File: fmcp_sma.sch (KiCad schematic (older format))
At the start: 52 parts, among them J101 Conn_Coaxial, J102 Conn_Coaxial, J103 Conn_Coaxial, J104 Conn_Coaxial, J105 Conn_Coaxial, J106 Conn_Coaxial, J201 FMCP_VITA57.4, U201 AT24C512C

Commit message: adding smas
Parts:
- removed J101, J102, J103, J104, J105, J106: Conn_Coaxial, Connector_Coaxial:MMCX_Molex_73415-0961_Horizontal_1.6mm-PCB, symbol Connector:Conn_Coaxial
- added C? (x4): 0.1uF, Capacitor_SMD:C_0201_0603Metric, symbol Device:C
- added J? (x14): Conn_Coaxial, Connector_Coaxial:MMCX_Molex_73415-0961_Horizontal_1.6mm-PCB, symbol Connector:Conn_Coaxial
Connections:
- net DPCLK_M2C_N0: now also J?.1 (In)
- net DPCLK_M2C_P0: now also J?.1 (In)
- net DP_C2M_N0: now also J?.1 (In)
- net DP_C2M_P0: now also J?.1 (In)
- net DP_M2C_N0: now also C?.2, J?.1 (In); no longer J201.C7 (DP0_M2C_N)
- net DP_M2C_P0: now also C?.2, J?.1 (In); no longer J201.C6 (DP0_M2C_P)
- net GND: now also J?.2 (Ext), J?.2 (Ext), J?.2 (Ext), J?.2 (Ext), J?.2 (Ext), J?.2 (Ext), J?.2 (Ext), J?.2 (Ext), J?.2 (Ext), J?.2 (Ext), J?.2 (Ext), J?.2 (Ext), J?.2 (Ext), J?.2 (Ext)
- net LA01_N: now also J?.1 (In)
- net LA01_P: now also J?.1 (In)
- net LA03_N: now reaches J201.G10 (LA03_N)
- net LA03_N: now also J?.1 (In)
- net LA00_P: now reaches J201.G6 (LA00_P_CC)
- net LA00_P: now also C102.2
- net LA00_N: now reaches J201.G7 (LA00_N_CC)
- net LA00_N: now also C101.2
- net LA03_P: now reaches J201.G9 (LA03_P)
- net LA03_P: now also J?.1 (In)
- net LA02_P: now reaches J201.H7 (LA02_P)
- net LA02_P: now also C?.2
- net LA02_N: now reaches J201.H8 (LA02_N)
- net LA02_N: now also C?.2
- net FPGA_CLK_C2M_C_N renamed LA00_C_N
- net LA00_C_N: now also J?.1 (In)
- net FPGA_CLK_C2M_C_P renamed LA00_C_P
- net LA00_C_P: now also J?.1 (In)
- new net: C?.1, J201.C6 (DP0_M2C_P)
- new net: C?.1, J201.C7 (DP0_M2C_N)
- new net LA02_C_N: C?.1, J?.1 (In)
- new net LA02_C_P: C?.1, J?.1 (In)
- no-connect marks 186 -> 282
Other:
- moved on the sheet: C101, C102, J201B, J201D, J201E, J201F

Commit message: added pdf
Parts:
- removed C202, C204, C207, C209: 10uF, Capacitor_SMD:C_0805_2012Metric, symbol Device:C
- removed C203, C205, C206, C208: 22uF, Capacitor_SMD:C_1210_3225Metric, symbol Device:C
- removed C210, C211, C212: C, Capacitor_SMD:C_0402_1005Metric, symbol Device:C
- removed R204, R207, R210: 0.1, Resistor_SMD:R_1210_3225Metric, symbol Device:R
- removed R205, R206, R208, R209, R211, R212: 10, Resistor_SMD:R_0402_1005Metric, symbol Device:R
- removed TP103, TP104: TestPoint, TestPoint:TestPoint_Loop_D2.50mm_Drill1.0mm, symbol Connector:TestPoint
- removed TP201, TP202, TP203: TestPoint_Probe, TestPoint:TestPoint_Pad_D1.0mm, symbol Connector:TestPoint_Probe
- removed U201: AT24C512C, Package_DFN_QFN:DFN-8-1EP_3x2mm_P0.5mm_EP1.3x1.5mm, symbol Memory_EEPROM:AT24CS64-MAHM
- added U101: M24C02-FDW, Package_SO:TSSOP-8_4.4x3mm_P0.65mm, symbol Memory_EEPROM:M24C02-FDW
- J101, J102, J104, J105, J106, J107, J108, J109, J110, J111, J112, J113, J114, J115: renamed from J?; footprint Connector_Coaxial:MMCX_Molex_73415-0961_Horizontal_1.6mm-PCB -> Connector_Coaxial:SMA_Amphenol_132134_Vertical; digikey# SAM8837-ND -> (none); manf Samtec -> (none); manf# MMCX-J-P-H-ST-EM1 -> (none); mouser# 200-MMCXJPHSTEM1 -> (none); rs# 158-7743 -> 253-0085
- gave numbers to parts that had none: 4
- renumbered C102 to C103, C101 to C104, C201 to C118, FID103 to FID102, FID105 to FID103, FID102 to FID104, FID104 to FID105, G102 to G101, G101 to G102, H103 to H102, H102 to H103, J201 to J103, R202 to R110, R203 to R111, TP101 to TP104, TP102 to TP105
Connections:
- net +3V3_FMCP: now also U101.8 (VCC)
- net GA0: now also U101.2 (E1)
- net GA1: now also U101.1 (E0)
- net GND: now also U101.3 (E2), U101.4 (VSS), U101.7 (~WC)
- net SCL: now also U101.6 (SCL)
- net SDA: now also U101.5 (SDA)
- net at J103.C6 (DP0_M2C_P): no longer C101.1
- net at J103.C7 (DP0_M2C_N): no longer C102.1
- net DP_M2C_C_P6: now reaches J103.B16 (DP6_M2C_P)
- net DP_M2C_C_P6: now also C101.1
- net DP_M2C_C_N6: now reaches J103.B17 (DP6_M2C_N)
- net DP_M2C_C_N6: now also C102.1
- net DPCLK_M2C_P1: now reaches J103.B20 (GBTCLK1_M2C_P)
- net DPCLK_M2C_P1: now also J104.1 (In)
- net DPCLK_M2C_N1: now reaches J103.B21 (GBTCLK1_M2C_N)
- net DPCLK_M2C_N1: now also J105.1 (In)
- net DP_C2M_P6: now reaches J103.B36 (DP6_C2M_P)
- net DP_C2M_P6: now also J101.1 (In)
- net DP_C2M_N6: now reaches J103.B37 (DP6_C2M_N)
- net DP_C2M_N6: now also J102.1 (In)
- net DPCLK_C2M_N3: no longer names the net of J103.L9 (GBTCLK3_M2C_N)
- net DPCLK_C2M_P3: no longer names the net of J103.L8 (GBTCLK3_M2C_P)
- net DPCLK_M2C_N0: no longer names the net of J103.D5 (GBTCLK0_M2C_N)
- net DPCLK_M2C_N0: no longer J105.1 (In)
- net DPCLK_M2C_P0: no longer names the net of J103.D4 (GBTCLK0_M2C_P)
- net DPCLK_M2C_P0: no longer J104.1 (In)
- net DP_C2M_N0: no longer names the net of J103.C3 (DP0_C2M_N)
- net DP_C2M_N0: no longer J102.1 (In)
- net DP_C2M_P0: no longer names the net of J103.C2 (DP0_C2M_P)
- net DP_C2M_P0: no longer J101.1 (In)
- net DP_M2C_N0 renamed DP_M2C_N6
- net DP_M2C_P0 renamed DP_M2C_P6
- net LA00_C_N renamed LA_N0
- net LA00_C_P renamed LA_P0
- net LA00_N renamed LA_C_N0
- net LA00_P renamed LA_C_P0
- net LA01_N renamed LA_N1
- net LA01_P renamed LA_P1
- net LA02_C_N renamed LA_N2
- net LA02_C_P renamed LA_P2
- net LA02_N renamed LA_C_N2
- net LA02_P renamed LA_C_P2
- net LA03_N renamed LA_N3
- net LA03_P renamed LA_P3
- no-connect marks 282 -> 284
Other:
- moved on the sheet: C101, C102, C103, C104, C105, C106, J101, J102, J103B, J103C, J103D, J103E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

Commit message: updated footprint
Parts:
- added J116, J117, J118, J119: Conn_Coaxial, KIT_Connector:SF2921-61345-1S, symbol Connector:Conn_Coaxial
- J101, J102, J104, J105, J106, J107: footprint Connector_Coaxial:SMA_Amphenol_132134_Vertical -> KIT_Connector:SF2921-61345-1S
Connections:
- net GND: now also J116.2 (Ext), J117.2 (Ext), J118.2 (Ext), J119.2 (Ext)
- new net Test_100_Ohm_N: J118.1 (In), J119.1 (In)
- new net Test_100_Ohm_P: J116.1 (In), J117.1 (In)
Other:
- note added: "100 Ohm Differential Microstrip"
- moved on the sheet: C118, J103F, R110, R111, U101

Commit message: routed
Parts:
- added C107, C108: 0.1uF, Capacitor_SMD:C_0201_0603Metric, symbol Device:C
- added C109: 1uF, Capacitor_SMD:C_0603_1608Metric, symbol Device:C
- added R101, R102, R103, R104, R105, R106, R107, R108, R109, R112: 0, Resistor_SMD:R_0201_0603Metric, symbol Device:R
- C118: footprint Capacitor_SMD:C_0402_1005Metric -> Capacitor_SMD:C_0603_1608Metric
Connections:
- net +3V3_FMCP: now also C109.1
- net DPCLK_M2C_N1: now also R104.1; no longer J103.B21 (GBTCLK1_M2C_N)
- net DPCLK_M2C_P1: now also R103.1; no longer J103.B20 (GBTCLK1_M2C_P)
- net DP_C2M_N6: now also R108.2; no longer J103.B37 (DP6_C2M_N)
- net DP_C2M_P6: now also R107.2; no longer J103.B36 (DP6_C2M_P)
- net GND: now also C109.2
- net LA_N1: now also R106.1; no longer J103.D9 (LA01_N_CC)
- net LA_N3: now also R102.1; no longer J103.G10 (LA03_N)
- net LA_P1: now also R105.1; no longer J103.D8 (LA01_P_CC)
- net LA_P3: now also R101.1; no longer J103.G9 (LA03_P)
- net Test_100_Ohm_N: now also C108.2, R112.2; no longer J118.1 (In), J119.1 (In)
- net Test_100_Ohm_P: now also C107.2, R109.2; no longer J116.1 (In), J117.1 (In)
- new net: J117.1 (In), R109.1
- new net: C107.1, J116.1 (In)
- new net: J119.1 (In), R112.1
- new net: C108.1, J118.1 (In)
- new net DPCLK_M2C_R_N1: J103.B21 (GBTCLK1_M2C_N), R104.2
- new net DPCLK_M2C_R_P1: J103.B20 (GBTCLK1_M2C_P), R103.2
- new net DP_C2M_R_N6: J103.B37 (DP6_C2M_N), R108.1
- new net DP_C2M_R_P6: J103.B36 (DP6_C2M_P), R107.1
- new net LA_R_N1: J103.D9 (LA01_N_CC), R106.2
- new net LA_R_N3: J103.G10 (LA03_N), R102.2
- new net LA_R_P1: J103.D8 (LA01_P_CC), R105.2
- new net LA_R_P3: J103.G9 (LA03_P), R101.2
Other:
- moved on the sheet: C101, C102, J101, J102, J104, J105, J106, J107, J108, J109, J110, J111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

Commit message: gerbers
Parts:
- added R113: 4.7k, Resistor_SMD:R_0603_1608Metric, symbol Device:R
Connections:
- net +3V3_FMCP: now also R113.1
- net PG_M2C: now also R113.2
- no-connect marks 284 -> 283
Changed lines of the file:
@@
 encoding utf-8
 Sheet 1 1
-Title "QSolid FMC+ SMA breakout"
-Date "2022-11-30"
+Title "FMC+ SMA breakout"
+Date "2022-12-07"
 Rev "1.0"
 Comp "Karlsruhe Institute of Technology (KIT)"
@@
 Wire Notes Line
 	7650 14750 8100 14750
-Text HLabel 20850 1900 2    50   Input ~ 0
-PG_M2C
-Wire Wire Line
-	20450 1900 20850 1900
 Wire Wire Line
 	14800 4800 14900 4800
@@
 NoConn ~ 5000 8450
 NoConn ~ 5000 8550
-Text Label 10550 15250 2    50   ~ 0
+Text Label 10750 15250 2    50   ~ 0
 SCL
-Text Label 10550 15150 2    50   ~ 0
+Text Label 10750 15150 2    50   ~ 0
 SDA
 NoConn ~ 12700 8950
@@
 Text Label 12350 4800 0    50   ~ 0
 SCL
-Text HLabel 10750 15250 2    50   Output ~ 0
-SCL
-Text HLabel 10750 15150 2    50   BiDi ~ 0
-SDA
 Text Label 8400 3800 0    50   ~ 0
 DPCLK_M2C_R_P1
@@
 NoConn ~ 15400 9100
 NoConn ~ 15400 9000
-NoConn ~ 17200 12200
 NoConn ~ 17200 12100
 NoConn ~ 17200 12000
@@
 	1    0    0    -1
 $EndComp
+$Comp
+L Device:R R?
+U 1 1 65461363
+P 21300 1700
+AR Path="/619BA206/65461363" Ref="R?"  Part="1"
+AR Path="/619269F2/65461363" Ref="R?"  Part="1"
+AR Path="/626146B8/65461363" Ref="R?"  Part="1"
+AR Path="/65461363" Ref="R113"  Part="1"
+F 0 "R113" H 21370 1746 50  0000 L CNN
+F 1 "4.7k" H 21370 1655 50  0000 L CNN
+F 2 "Resistor_SMD:R_0603_1608Metric" V 21230 1700 50  0001 C CNN
+F 3 "~" H 21300 1700 50  0001 C CNN
+	1    21300 1700
+	1    0    0    -1
+$EndComp
+Wire Wire Line
+	21300 1850 21300 1900
+Wire Wire Line
+	21300 1900 20450 1900
+$Comp
+L KIT_Power:+3V3_FMCP #PWR?
+U 1 1 655BE826
+P 21300 1550
+F 0 "#PWR?" H 21300 1400 50  0001 C CNN
+F 1 "+3V3_FMCP" H 21315 1723 50  0000 C CNN
+F 2 "" H 21300 1550 50  0001 C CNN
+F 3 "" H 21300 1550 50  0001 C CNN
+	1    21300 1550
+	1    0    0    -1
+$EndComp
+Text Label 20700 1900 0    50   ~ 0
+PG_M2C
 $EndSCHEMATC

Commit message: modified footprint for screw on sma conn@
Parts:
- added J120, J121: Conn_Coaxial, KIT_Connector:SF2921-61345-1S, symbol Connector:Conn_Coaxial
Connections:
- net GND: now also J120.2 (Ext), J121.2 (Ext)
- new net Test_50_Ohm: J120.1 (In), J121.1 (In)
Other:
- note added: "50 Ohm Microstrip"
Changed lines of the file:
@@
 Sheet 1 1
 Title "FMC+ SMA breakout"
-Date "2022-12-07"
+Date "2022-12-09"
 Rev "1.0"
 Comp "Karlsruhe Institute of Technology (KIT)"
 Comment1 "Institute for Data Processing and Electronics (IPE)"
-Comment2 "Luis Ardila"
-Comment3 ""
+Comment2 "Robert Gartmann, Lukas Scheller"
+Comment3 "Luis Ardila, Marvin Fuchs, "
 Comment4 ""
 $EndDescr
@@
 Text Label 20700 1900 0    50   ~ 0
 PG_M2C
+$Comp
+L Connector:Conn_Coaxial J121
+U 1 1 63992A69
+P 22300 12000
+F 0 "J121" H 22400 11929 50  0000 L CNN
+F 1 "Conn_Coaxial" H 22400 11884 50  0001 L CNN
+F 2 "KIT_Connector:SF2921-61345-1S" H 22300 12000 50  0001 C CNN
+F 3 " ~" H 22300 12000 50  0001 C CNN
+F 4 "" H 22300 12000 50  0001 C CNN "manf"
+F 5 "" H 22300 12000 50  0001 C CNN "manf#"
+F 6 "" H 22300 12000 50  0001 C CNN "mouser#"
+F 7 "" H 22300 12000 50  0001 C CNN "digikey#"
+F 8 "253-0085" H 22300 12000 50  0001 C CNN "rs#"
+	1    22300 12000
+	1    0    0    -1
+$EndComp
+$Comp
+L Connector:Conn_Coaxial J120
+U 1 1 63992A74
+P 19100 12000
+F 0 "J120" H 19200 11929 50  0000 L CNN
+F 1 "Conn_Coaxial" H 19200 11884 50  0001 L CNN
+F 2 "KIT_Connector:SF2921-61345-1S" H 19100 12000 50  0001 C CNN
+F 3 " ~" H 19100 12000 50  0001 C CNN
+F 4 "" H 19100 12000 50  0001 C CNN "manf"
+F 5 "" H 19100 12000 50  0001 C CNN "manf#"
+F 6 "" H 19100 12000 50  0001 C CNN "mouser#"
+F 7 "" H 19100 12000 50  0001 C CNN "digikey#"
+F 8 "253-0085" H 19100 12000 50  0001 C CNN "rs#"
+	1    19100 12000
+	-1   0    0    -1
+$EndComp
+$Comp
+L power:GND #PWR?
+U 1 1 63992A7A
+P 19100 12200
+F 0 "#PWR?" H 19100 11950 50  0001 C CNN
+F 1 "GND" H 19105 12027 50  0000 C CNN
+F 2 "" H 19100 12200 50  0001 C CNN
+F 3 "" H 19100 12200 50  0001 C CNN
+	1    19100 12200
+	-1   0    0    -1
+$EndComp
+$Comp
+L power:GND #PWR?
+U 1 1 63992A80
+P 22300 12200
+F 0 "#PWR?" H 22300 11950 50  0001 C CNN
+F 1 "GND" H 22305 12027 50  0000 C CNN
+F 2 "" H 22300 12200 50  0001 C CNN
+F 3 "" H 22300 12200 50  0001 C CNN
+	1    22300 12200
+	1    0    0    -1
+$EndComp
+Text Notes 20000 11750 0    98   ~ 0
+50 Ohm Microstrip
+Text Label 21000 12000 2    50   ~ 0
+Test_50_Ohm
+Wire Notes Line
+	18650 11500 22850 11500
+Wire Notes Line
+	18650 12600 22850 12600
+Wire Wire Line
+	19300 12000 22100 12000
+Wire Notes Line
+	22850 12600 22850 11500
+Wire Notes Line
+	18650 11500 18650 12600
 $EndSCHEMATC

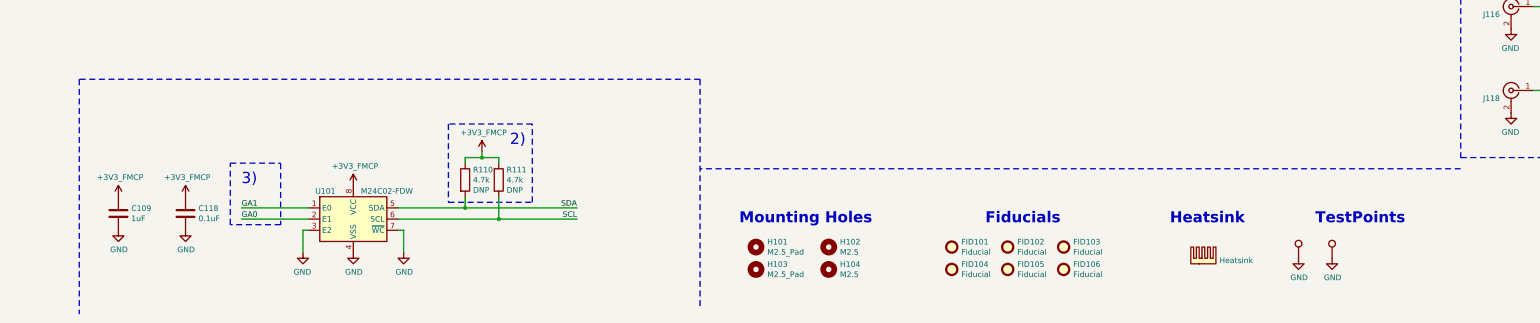
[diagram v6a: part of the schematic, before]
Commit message: re-pour zones with 0.3 clearance and 1mm for traces only
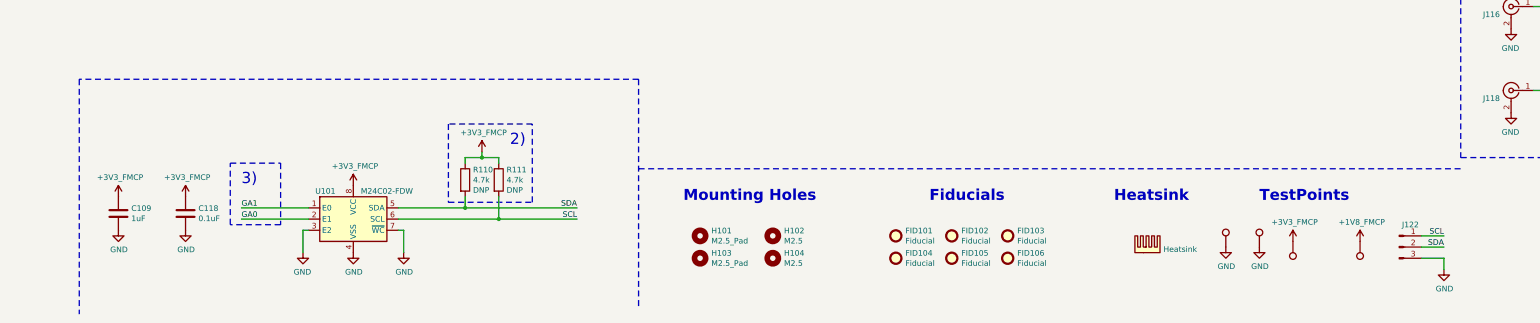
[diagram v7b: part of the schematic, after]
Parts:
- added J122: Conn_01x03_Male, Connector_PinHeader_2.54mm:PinHeader_1x03_P2.54mm_Vertical, symbol Connector:Conn_01x03_Male
- added TP101, TP102: TestPoint, TestPoint:TestPoint_Loop_D2.50mm_Drill1.0mm, symbol Connector:TestPoint
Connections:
- net +1V8_FMCP: now also TP102.1
- net +3V3_FMCP: now also TP101.1
- net GND: now also J122.3 (Pin_3)
- net SCL: now also J122.1 (Pin_1)
- net SDA: now also J122.2 (Pin_2)
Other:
- moved on the sheet: FID101, FID102, FID103, FID104, FID105, FID106, H101, H102, H103, H104
